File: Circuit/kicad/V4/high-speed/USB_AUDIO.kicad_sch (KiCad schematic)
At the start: 40 parts, among them SW2 SW_Push, SW3 SW_Push, SW4 SW_Push, U64 PCM2704CDBR, U65 TPA6203A1DGN, Y3 5MHz

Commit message: high speed first step
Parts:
- renumbered C120 to C54, C122 to C55, C134 to C56, C135 to C57, C136 to C58, C124 to C59, C131 to C60, C127 to C61, C125 to C62, C128 to C63, C129 to C64, C132 to C65, C137 to C66, C126 to C67, C121 to C68, C130 to C69, C133 to C70, C123 to C71, CT9 to CT7, R110 to R76, R108 to R77, R109 to R78, R106 to R79, R107 to R80, R115 to R81, R117 to R82, R113 to R83, R112 to R84, R116 to R85, R118 to R86, R119 to R87, R111 to R88, R114 to R89, U64 to U25, U65 to U26

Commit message: kicad: high speed V2.2 Circuit finish psu bom update
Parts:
- added R121: 0R, Resistor_SMD:R_0805_2012Metric, symbol Device:R
- C56: renamed from C54; Cikkszám (none) -> 100.011.31; Link (none) -> https://www.hestore.hu/prod_10001131.html
- C57: renamed from C55; Cikkszám (none) -> 100.011.31; Link (none) -> https://www.hestore.hu/prod_10001131.html
- C58: renamed from C56; value 1uf -> 22nf c0g; Cikkszám (none) -> 100.011.30; Link (none) -> https://www.hestore.hu/prod_10001130.html
- C59: renamed from C57; value 1uf -> 100nf; Cikkszám (none) -> 100.011.22; Link (none) -> https://www.hestore.hu/prod_10001122.html
- C60: renamed from C58; Cikkszám (none) -> 100.277.53; Link (none) -> https://www.hestore.hu/prod_10027753.html
- C61: renamed from C59; Cikkszám (none) -> 100.277.53; Link (none) -> https://www.hestore.hu/prod_10027753.html
- C62: renamed from C60; value 10uf -> 10uF; Cikkszám (none) -> 100.230.37; Link (none) -> https://www.hestore.hu/prod_10023037.html
- C63: renamed from C61; Cikkszám (none) -> 100.277.53; Link (none) -> https://www.hestore.hu/prod_10027753.html
- C64: renamed from C62; Cikkszám (none) -> 100.277.53; Link (none) -> https://www.hestore.hu/prod_10027753.html
- C65: renamed from C63; Cikkszám (none) -> 100.277.53; Link (none) -> https://www.hestore.hu/prod_10027753.html
- C66: renamed from C64; value 100uf -> 100uF; Cikkszám (none) -> 100.286.19; Link (none) -> https://www.hestore.hu/prod_10028619.html
- C67: renamed from C65; Cikkszám (none) -> 100.277.53; Link (none) -> https://www.hestore.hu/prod_10027753.html
- C68: renamed from C66; value 0.022-μF -> 22nf c0g; Cikkszám (none) -> 100.011.30; Link (none) -> https://www.hestore.hu/prod_10001130.html
- C69: renamed from C67; value 0.022-μF -> 22nf c0g; Cikkszám (none) -> 100.011.30; Link (none) -> https://www.hestore.hu/prod_10001130.html
- C70: renamed from C68; Cikkszám (none) -> 100.277.53; Link (none) -> https://www.hestore.hu/prod_10027753.html
- C71: renamed from C69; value 100uf -> 100uF; Cikkszám (none) -> 100.286.19; Link (none) -> https://www.hestore.hu/prod_10028619.html
- C72: renamed from C70; Cikkszám (none) -> 100.277.53; Link (none) -> https://www.hestore.hu/prod_10027753.html
- C73: renamed from C71; value 0.022-μF -> 22nf c0g; Cikkszám (none) -> 100.011.30; Link (none) -> https://www.hestore.hu/prod_10001130.html
- CT9: renamed from CT7; value 10uf -> 10uF; Cikkszám (none) -> 100.230.37; Link (none) -> https://www.hestore.hu/prod_10023037.html
- R118: renamed from R76; Cikkszám (none) -> 100.011.55; Link (none) -> https://www.hestore.hu/prod_10001155.html
- R119: renamed from R77; value 22 -> 22R; Cikkszám (none) -> 100.012.50; Link (none) -> https://www.hestore.hu/prod_10001250.html
- R120: renamed from R78; value 22Ω -> 22R; Cikkszám (none) -> 100.012.50; Link (none) -> https://www.hestore.hu/prod_10001250.html
- R122: renamed from R79; value 1.5-kΩ -> 1.5K; Cikkszám (none) -> 100.011.58; Link (none) -> https://www.hestore.hu/prod_10001158.html
- R123: renamed from R80; value 1.5-kΩ -> 1.5K; Cikkszám (none) -> 100.011.58; Link (none) -> https://www.hestore.hu/prod_10001158.html
- R124: renamed from R81; Cikkszám (none) -> 100.011.45; Link (none) -> https://www.hestore.hu/prod_10001145.html
- R125: renamed from R82; Cikkszám (none) -> 100.011.45; Link (none) -> https://www.hestore.hu/prod_10001145.html
- R126: renamed from R83; value 330 -> 330R; Cikkszám (none) -> 100.011.70; Link (none) -> https://www.hestore.hu/prod_10001170.html
- R127: renamed from R84; value 16 -> 16R; Cikkszám (none) -> 100.491.03; Link (none) -> https://www.hestore.hu/prod_10049103.html
- R128: renamed from R85; Cikkszám (none) -> 100.011.45; Link (none) -> https://www.hestore.hu/prod_10001145.html
- R129: renamed from R86; Cikkszám (none) -> 100.011.45; Link (none) -> https://www.hestore.hu/prod_10001145.html
- R130: renamed from R87; Cikkszám (none) -> 100.011.45; Link (none) -> https://www.hestore.hu/prod_10001145.html
- R131: renamed from R88; value 16 -> 16R; Cikkszám (none) -> 100.491.03; Link (none) -> https://www.hestore.hu/prod_10049103.html
- R132: renamed from R89; value 330 -> 330R; Cikkszám (none) -> 100.011.70; Link (none) -> https://www.hestore.hu/prod_10001170.html
- SPEAKER1: Cikkszám (none) -> 100.385.23; Link (none) -> https://www.hestore.hu/prod_10038523.html
- SW2, SW3, SW4: Cikkszám (none) -> 100.409.03; Link (none) -> https://www.hestore.hu/prod_10040903.html
- U27: renamed from U25; footprint psu:SSOP28 -> panel:SSOP28; Availability In Stock -> (none); Check_prices https://www.snapeda.com/parts/PCM2704C/Texas+Instruments/vi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 -> (none); Cikkszám (none) -> 100.490.95; Description_1 Stereo Audio DAC with USB Interface, Single-Ended Headphone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 -> (none); Link (none) -> https://www.hestore.hu/prod_10049095.html; MF Texas Instruments -> (none); MP PCM2704C -> (none); Package None -> (none); Price None -> (none); SnapEDA_Link https://www.snapeda.com/parts/PCM2704C/Texas+Instruments/vi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 -> (none)
- U28: renamed from U26; Cikkszám (none) -> 100.490.98; Link (none) -> https://www.hestore.hu/prod_10049098.html
- Y2: renamed from Y3; value 5MHz -> 12MHz; Cikkszám (none) -> 100.213.87; Link (none) -> https://www.hestore.hu/prod_10021387.html
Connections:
- net GND: now also R121.1; no longer C70.1, R126.1, R127.1, R130.2, R131.1, R132.1, U27.12 (AGNDL), U27.17 (AGNDR), U28.7 (GND), U28.9 (GND)
- net TPA-ON renamed TPA_ON
- new net GNDA: C70.1, R121.2, R126.1, R127.1, R130.2, R131.1, R132.1, U27.12 (AGNDL), U27.17 (AGNDR), U28.7 (GND), U28.9 (GND)
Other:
- moved on the sheet: C58

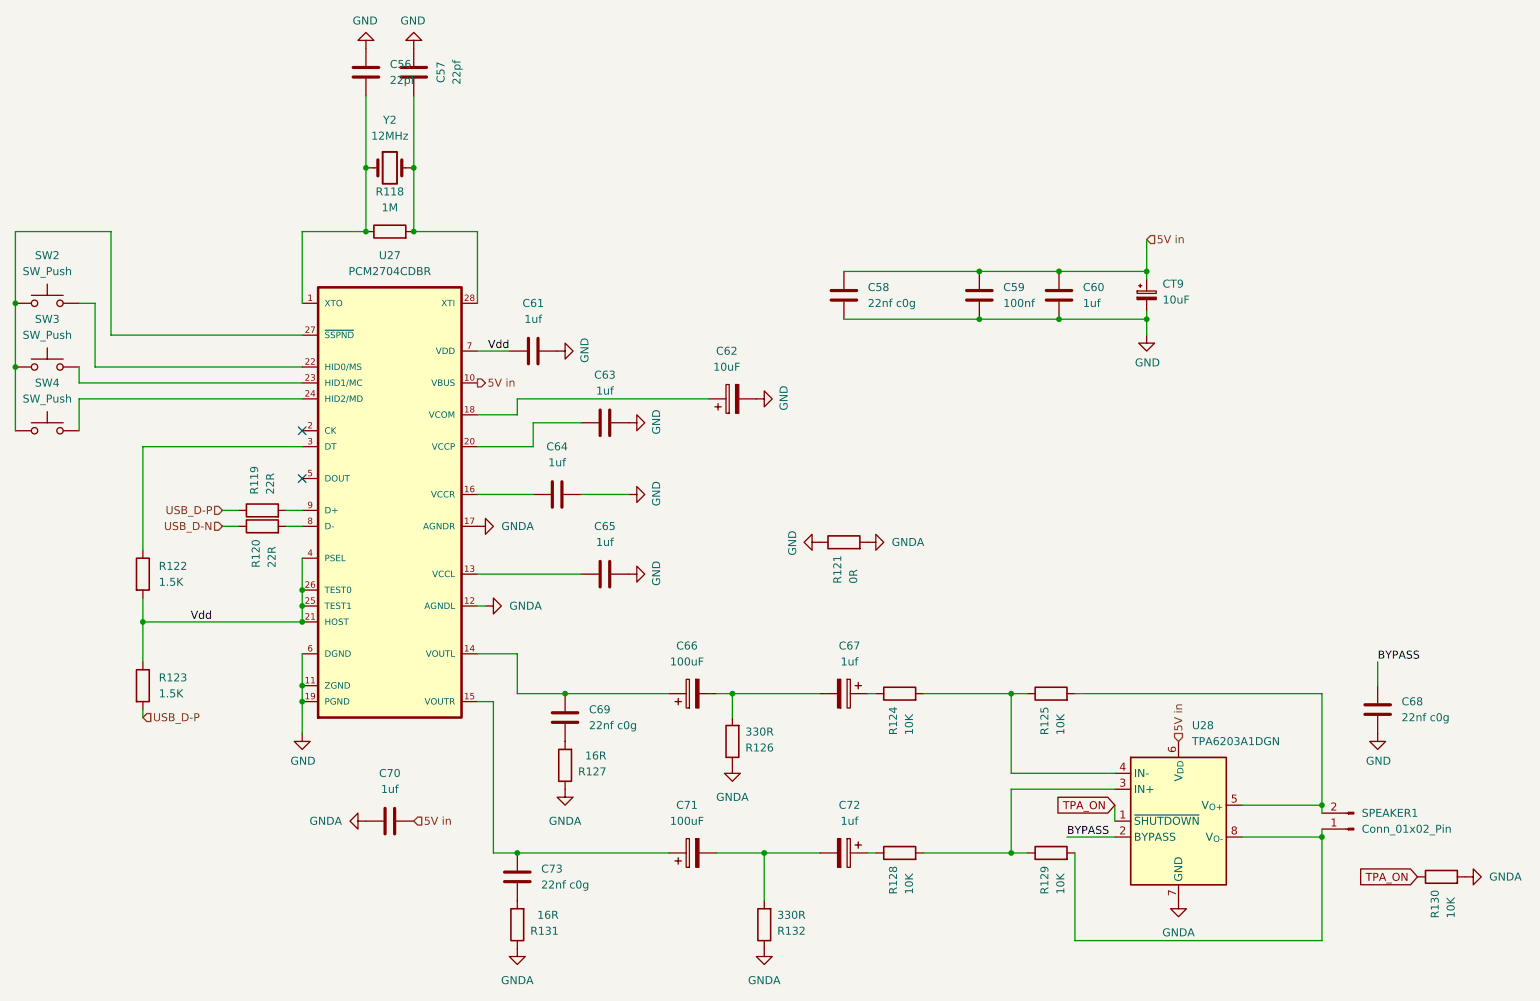
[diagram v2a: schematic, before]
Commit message: finished high-speed panel schematic and first try to doute gpios
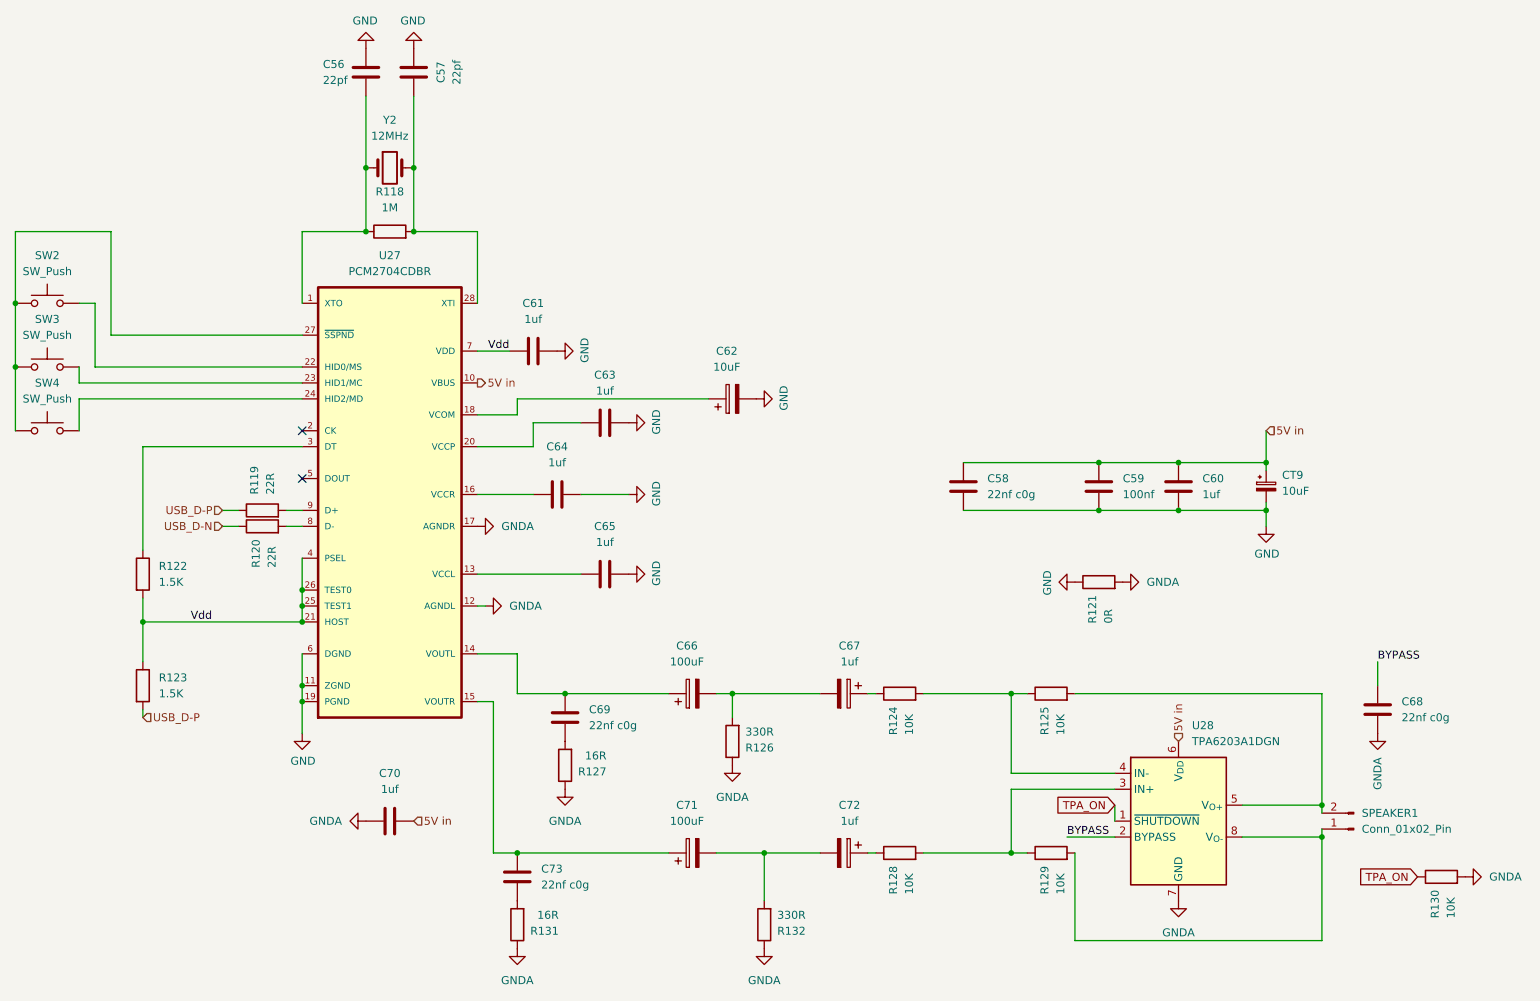
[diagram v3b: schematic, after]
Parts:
- C62, CT9: footprint Capacitor_Tantalum_SMD:CP_EIA-3528-21_Kemet-B -> Capacitor_Tantalum_SMD:CP_EIA-3216-18_Kemet-A_HandSolder
- C66, C71: footprint Capacitor_Tantalum_SMD:CP_EIA-7343-31_Kemet-D -> Capacitor_Tantalum_SMD:CP_EIA-3528-21_Kemet-B
- SW2, SW3, SW4: footprint Connector_PinHeader_2.54mm:PinHeader_1x02_P2.54mm_Vertical -> panel:tact-smd sw
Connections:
- net GND: no longer C68.2
- net GNDA: now also C68.2
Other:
- moved on the sheet: C58, C59, C60, CT9, R121

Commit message: pcb update
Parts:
- removed C70: 1uf, Capacitor_SMD:C_0805_2012Metric, symbol Device:C
- removed R121: 0R, Resistor_SMD:R_0805_2012Metric, symbol Device:R
- removed R123: 1.5K, Resistor_SMD:R_0805_2012Metric, symbol Device:R
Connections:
- net GNDA is gone; now on net GND: C68.2, R126.1, R127.1, R130.2, R131.1, R132.1, U27.12 (AGNDL), U27.17 (AGNDR), U28.7 (GND), U28.9 (GND)
